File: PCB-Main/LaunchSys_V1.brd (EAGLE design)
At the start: 30.5 x 35.6 mm, 4 parts

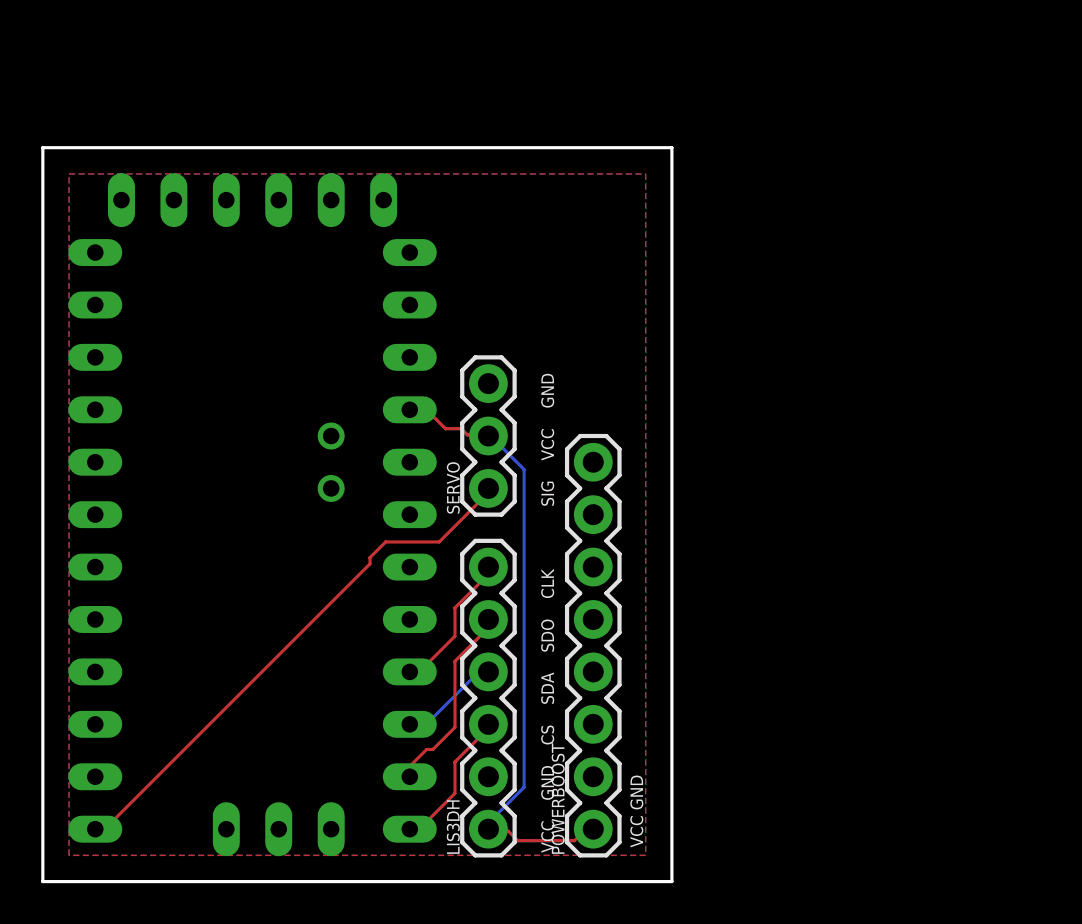
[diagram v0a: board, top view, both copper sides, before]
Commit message: Updated launch board to include TIP120 power transistor and switch for controlling solenoid
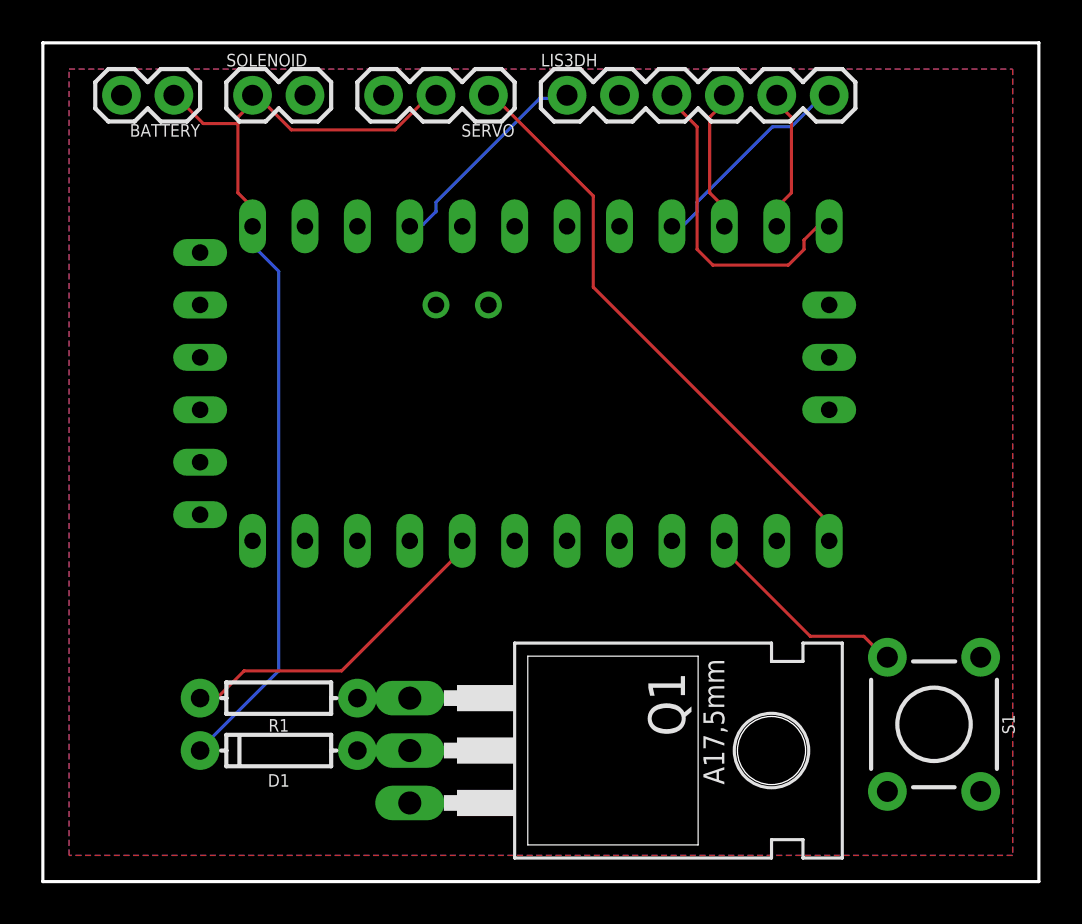
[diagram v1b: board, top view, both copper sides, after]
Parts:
- removed POWERBOOST: (no value), SparkFun-Connectors:1X08
- added BATTERY, SOLENOID: (no value), SparkFun-Connectors:1X02
- added D1: 200mA/100V/1V, SparkFun-DiscreteSemi:DIODE-1N4148
- added Q1: TIP120, transistor-power:TO220AH
- added R1: 2.2k, SparkFun-Resistors:AXIAL-0.3
- added S1: MOMENTARY-SWITCH-SPST-PTH-6.0MM, SparkFun-Switches:TACTILE_SWITCH_PTH_6.0MM
- moved LIS3DH 35.8 mm to (25.4, 38.1), turned to 0 degrees
- moved SERVO 19.1 mm to (21.6, 38.1), turned to 180 degrees
- moved U$1 9.25 mm to (16.5, 21.6), turned to 90 degrees
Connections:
- net N$5 renamed D9
- new net N$1: R1.P$2, U$1.D2
- new net N$2: Q1.B, R1.P$1
- new net N$3: S1.3, U$1.D7
- new net N$4: D1.A, Q1.C
- new net V_BATT: BATTERY.1, D1.C, SERVO.2, SOLENOID.1, U$1.RAW
- net GND: now also BATTERY.2, Q1.E, S1.1, SOLENOID.2; no longer POWERBOOST.2
- net VCC: now also U$1.VCC; no longer POWERBOOST.1, SERVO.2, U$1.RAW
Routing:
- net V_BATT: track 0.00 -> 48.8 mm
- net VCC: track 29.7 -> 10.5 mm
- net N$1: track 0.00 -> 16.2 mm
- net N$3: track 0.00 -> 10.5 mm
- net CS: track 6.99 -> 15.8 mm
- net SCL: track 6.99 -> 10.6 mm
- net N$2: track 0.00 -> 2.68 mm
- net N$4: track 0.00 -> 2.60 mm
- net SDO: track 9.39 -> 7.00 mm
- net D9: track 26.2 -> 28.5 mm
- net SDA: track 4.86 -> 7.00 mm
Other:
- board size 30.5 x 35.6 mm -> 48.3 x 40.6 mm
- board text added: "Rocket Control Ver 0.2 David Smith 04/14/2019"
- board text removed: "Rocket Control Ver 0.1 David Smith 02/15/2019"
- board text removed: "SIG VCC GND"
- board text removed: "VCC GND"
- board text removed: "VCC GND CS SDA SDO CLK"
